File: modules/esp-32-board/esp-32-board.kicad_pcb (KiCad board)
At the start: 2 copper layers, 53.4 x 68.6 mm, 37 parts, among them J1 ESP-PROG-Program, J2 MainConnector, J3 ESP-PROG-Debug, J4 Conn_01x06, J5 Barrel_Jack_MountingPin, J7 USB_B_Micro, Q1 BCR129S, SW1 SW_Push, SW2 SW_Push, U1 ESP32-WROOM-32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

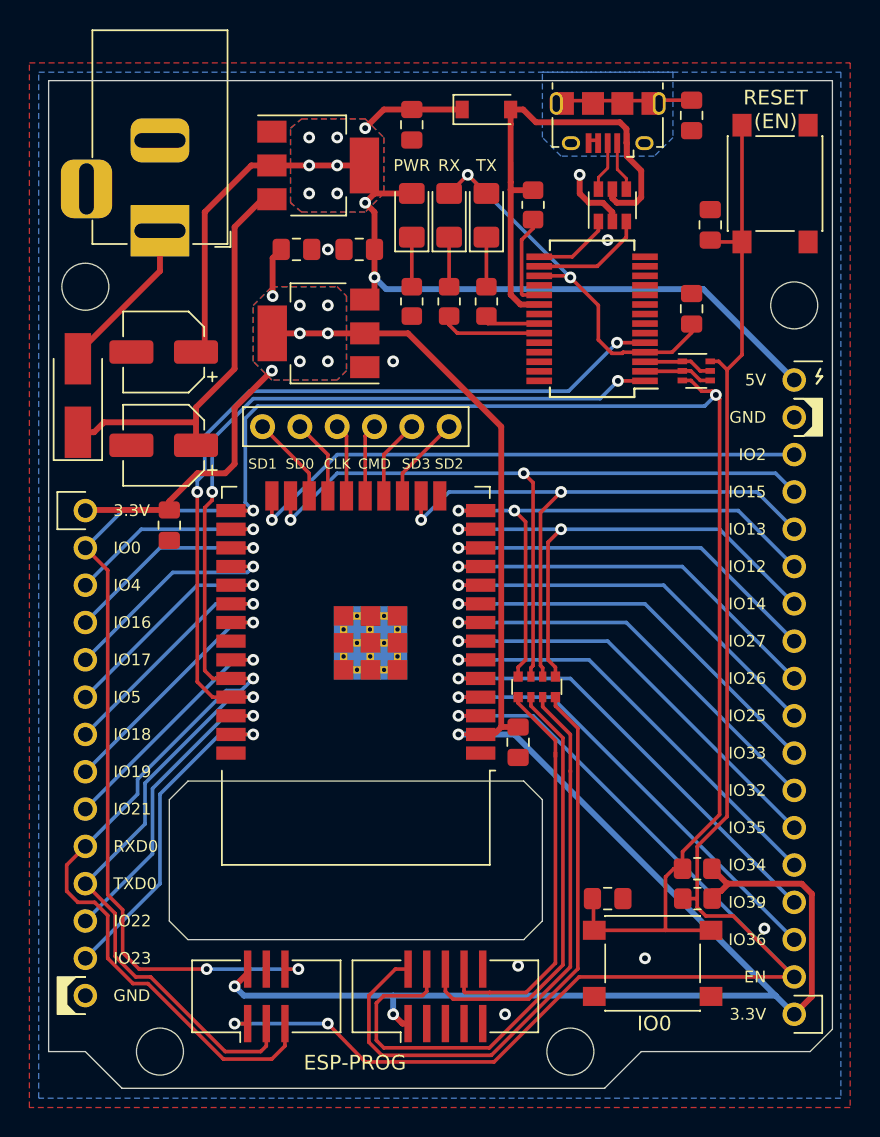
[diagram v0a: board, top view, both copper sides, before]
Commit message: Replace MainConnector with ArduinoFootprint and separate headers
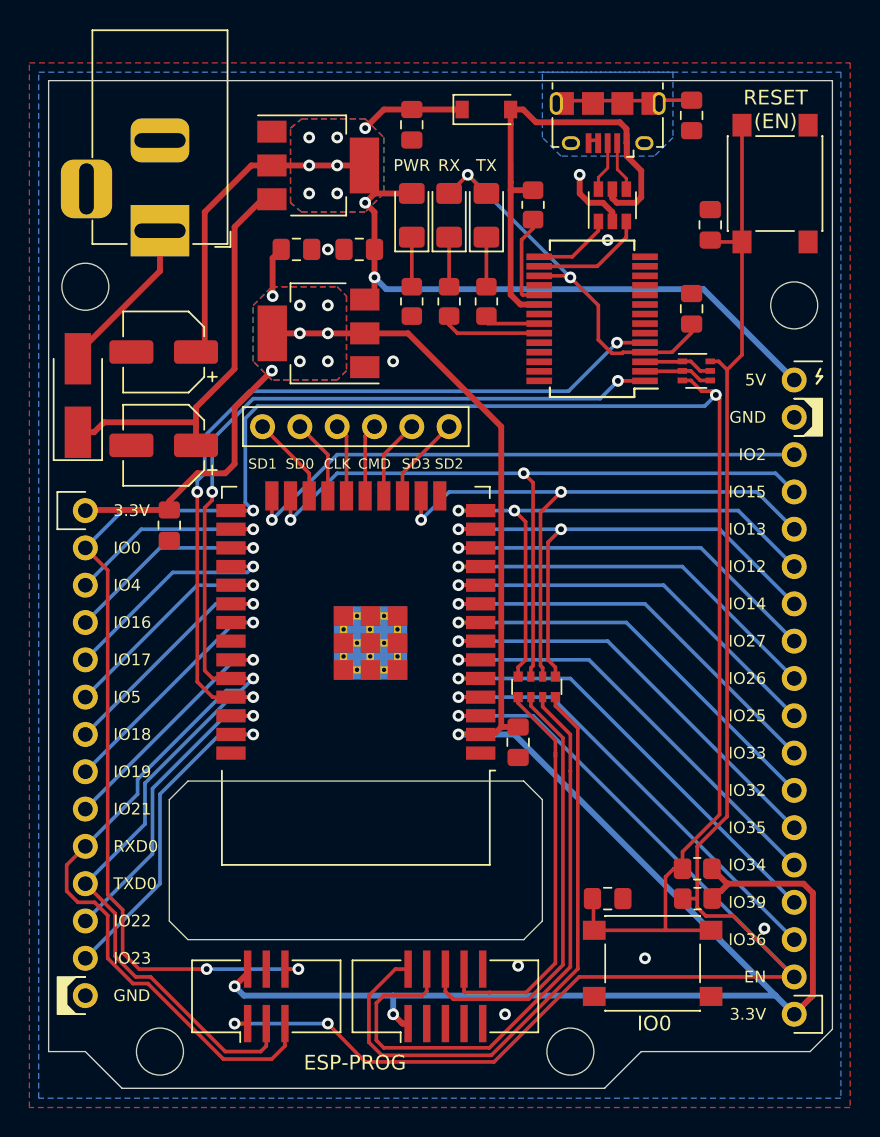
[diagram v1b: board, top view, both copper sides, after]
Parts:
- added J1: Conn_01x14_Female, Connector_PinSocket_2.54mm:PinSocket_1x14_P2.54mm_Vertical, F.Cu at (132.1, 50.8)
- added J2: Conn_01x18_Female, Connector_PinSocket_2.54mm:PinSocket_1x18_P2.54mm_Vertical, F.Cu at (180.3, 41.9)
- N1: renamed from J2; value MainConnector -> ArduinoFootprint; footprint project_components:MainConnector -> project_components:ArduinoFootprint
- R2: value 2.2k Ohm -> 2.2 kOhm
- R5, R6: value 10k Ohm -> 10 kOhm
- renumbered J4 to J3, J7 to J4, J1 to J6, J3 to J7

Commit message: Add custom symbols/footprints to project_components
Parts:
- J5: footprint Connector_BarrelJack:BarrelJack_CLIFF_FC68148_Horizontal -> project_components:BarrelJack_CLIFF_FC68148_Horizontal
- J6: footprint Connector_IDC:IDC-Header_2x03_P1.27mm_Vertical_SMD -> project_components:IDC-Header_2x03_P1.27mm_Vertical_SMD
- J7: footprint Connector_IDC:IDC-Header_2x05_P1.27mm_Vertical_SMD -> project_components:IDC-Header_2x05_P1.27mm_Vertical_SMD
- N1: value ArduinoFootprint -> Arduino Footprint
- SW1, SW2: footprint Button_Switch_SMD:SW_Push_1P1T_NO_6x6mm_H4.3mm -> project_components:SW_Push_1P1T_NO_6x6mm_H4.3mm
- U1: footprint RF_Module:ESP32-WROOM-32-ThermalVias -> project_components:ESP32-WROOM-32-ThermalVias
